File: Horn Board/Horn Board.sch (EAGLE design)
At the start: 11 parts, among them K1 RELAY-SPDT-JZC-11F, T1 2N2222

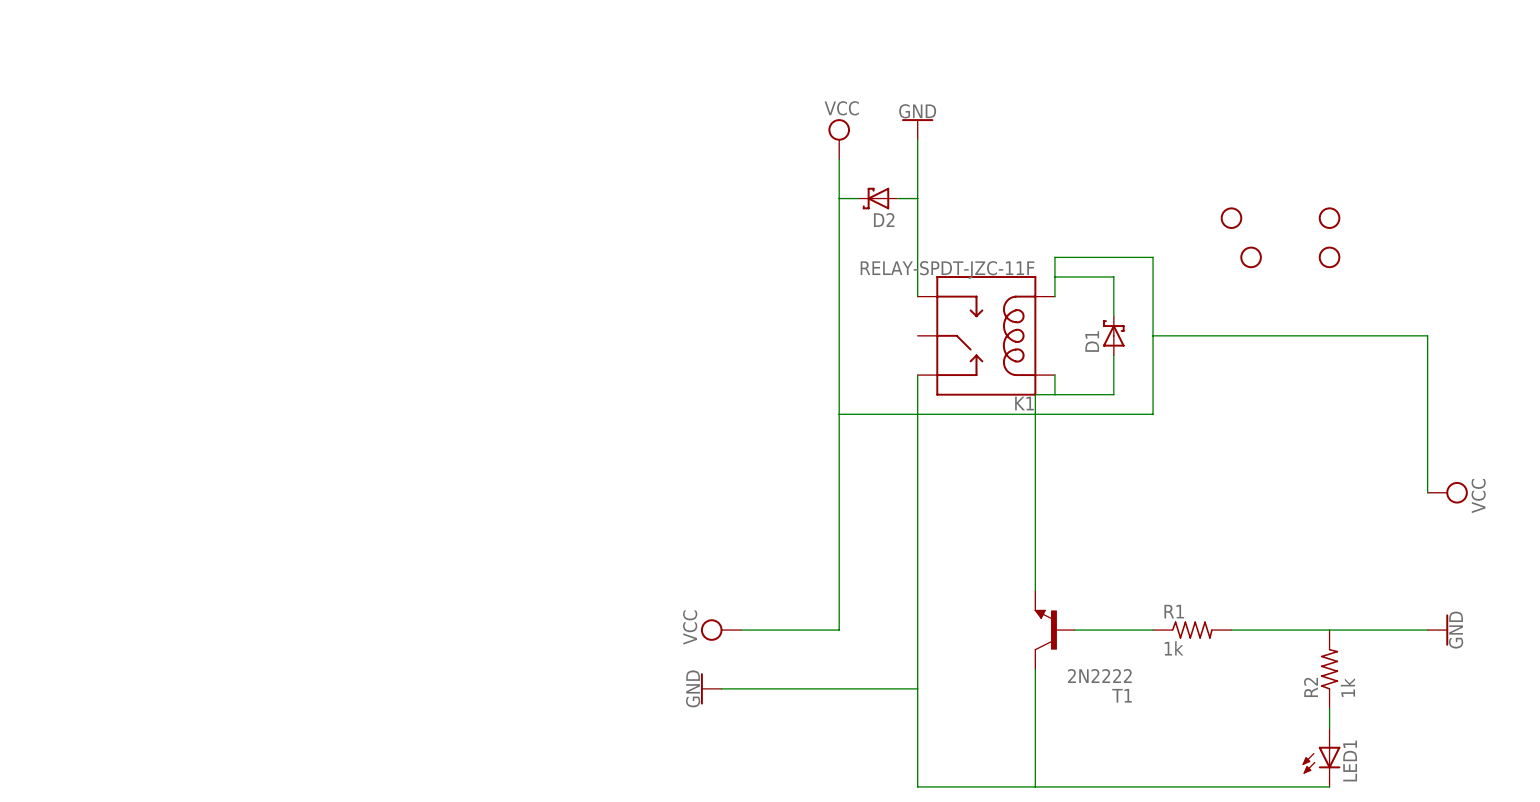
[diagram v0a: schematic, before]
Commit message: Added Connectors to horn board
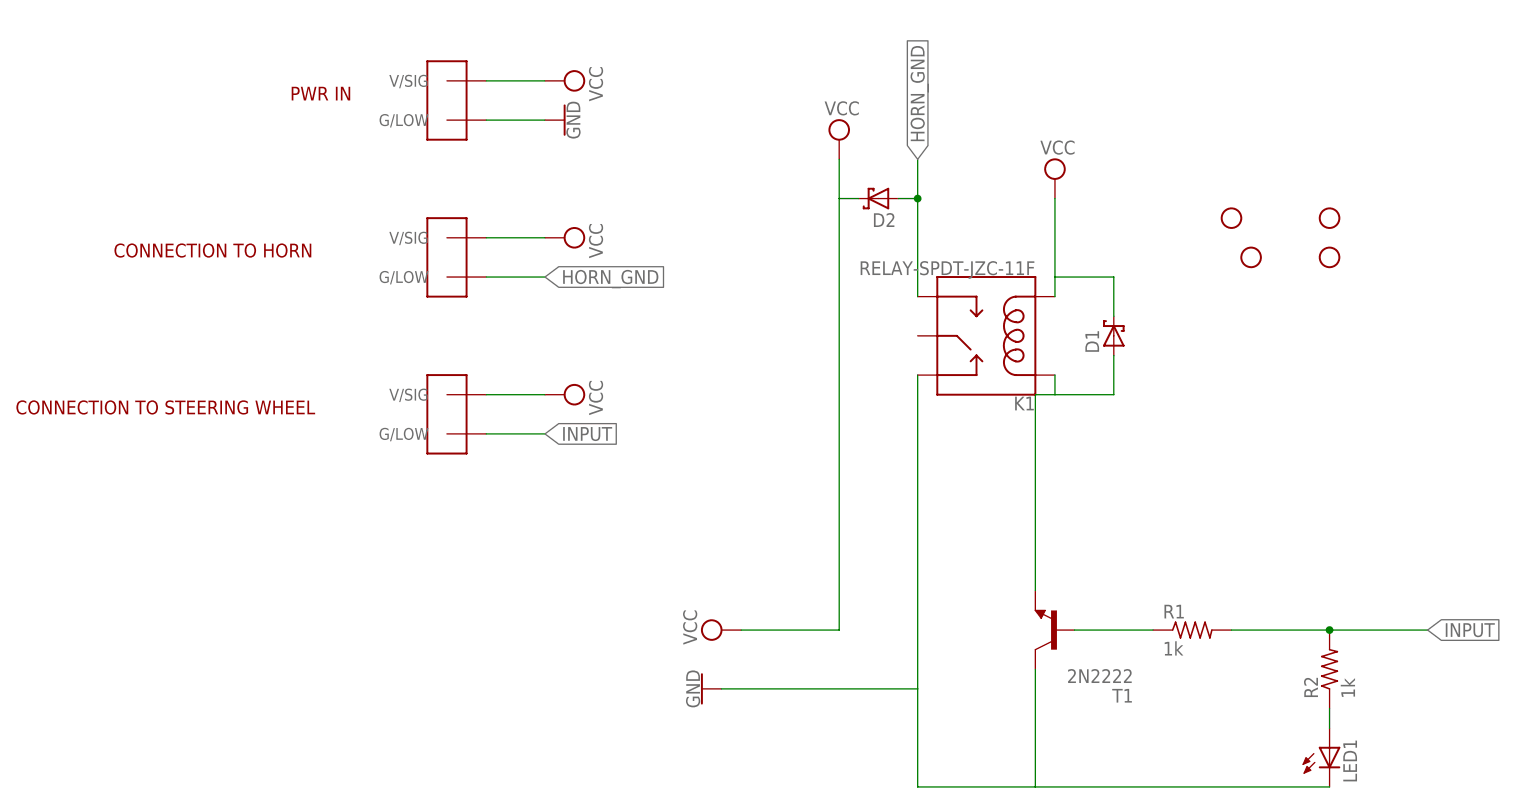
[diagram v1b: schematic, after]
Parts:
- added U$1, U$2, U$8: TE770966, Shell2013(1):TE770966
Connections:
- new net HORN_GND: D2.A, K1.NO, U$1.G/LOW
- new net INPUT: R1.2, R2.2, U$2.G/LOW
- net GND: now also U$8.G/LOW; no longer D2.A, K1.NO, R1.2, R2.2
- net VCC: now also U$1.V/SIG, U$2.V/SIG, U$8.V/SIG
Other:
- note added: "CONNECTION TO HORN"
- note added: "CONNECTION TO STEERING WHEEL"
- note added: "PWR IN"
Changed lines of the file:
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@@
 <?xml version="1.0" encoding="utf-8"?>
 <!DOCTYPE eagle SYSTEM "eagle.dtd">
-<eagle version="8.3.2">
+<eagle version="8.4.1">
 <drawing>
 <settings>
@@
 <layers>
 <layer number="1" name="Top" color="4" fill="1" visible="no" active="no"/>
+<layer number="2" name="Route2" color="1" fill="3" visible="no" active="no"/>
+<layer number="3" name="Route3" color="4" fill="3" visible="no" active="no"/>
+<layer number="14" name="Route14" color="1" fill="6" visible="no" active="no"/>
+<layer number="15" name="Route15" color="4" fill="6" visible="no" active="no"/>
 <layer number="16" name="Bottom" color="1" fill="1" visible="no" active="no"/>
 <layer number="17" name="Pads" color="2" fill="1" visible="no" active="no"/>
@@
 <part name="R2" library="adafruit" library_urn="urn:adsk.eagle:library:420" deviceset="R-US_" device="0204/2V" value="1k"/>
 <part name="T1" library="adafruit" library_urn="urn:adsk.eagle:library:420" deviceset="2N2222" device=""/>
-<part name="SUPPLY4" library="supply2" library_urn="urn:adsk.eagle:library:372" deviceset="VCC" device=""/>
 <part name="SUPPLY5" library="supply2" library_urn="urn:adsk.eagle:library:372" deviceset="VCC" device=""/>
 <part name="SUPPLY6" library="supply2" library_urn="urn:adsk.eagle:library:372" deviceset="VCC" device=""/>
-<part name="GND1" library="SparkFun-PowerSymbols" library_urn="urn:adsk.eagle:library:530" deviceset="GND" device=""/>
 <part name="GND2" library="SparkFun-PowerSymbols" library_urn="urn:adsk.eagle:library:530" deviceset="GND" device=""/>
-<part name="GND3" library="SparkFun-PowerSymbols" library_urn="urn:adsk.eagle:library:530" deviceset="GND" device=""/>
 <part name="H1" library="SparkFun-Hardware" library_urn="urn:adsk.eagle:library:519" deviceset="STAND-OFF" device="" package3d_urn="urn:adsk.eagle:package:38630/1"/>
 <part name="H2" library="SparkFun-Hardware" library_urn="urn:adsk.eagle:library:519" deviceset="STAND-OFF" device="" package3d_urn="urn:adsk.eagle:package:38630/1"/>
 <part name="H3" library="SparkFun-Hardware" library_urn="urn:adsk.eagle:library:519" deviceset="STAND-OFF" device="" package3d_urn="urn:adsk.eagle:package:38630/1"/>
 <part name="H4" library="SparkFun-Hardware" library_urn="urn:adsk.eagle:library:519" deviceset="STAND-OFF" device="" package3d_urn="urn:adsk.eagle:package:38630/1"/>
+<part name="U$8" library="Shell2013(1)" deviceset="TE770966" device=""/>
+<part name="U$1" library="Shell2013(1)" deviceset="TE770966" device=""/>
+<part name="U$2" library="Shell2013(1)" deviceset="TE770966" device=""/>
+<part name="SUPPLY1" library="supply2" library_urn="urn:adsk.eagle:library:372" deviceset="VCC" device=""/>
+<part name="SUPPLY2" library="supply2" library_urn="urn:adsk.eagle:library:372" deviceset="VCC" device=""/>
+<part name="GND1" library="SparkFun-PowerSymbols" library_urn="urn:adsk.eagle:library:530" deviceset="GND" device=""/>
+<part name="SUPPLY3" library="supply2" library_urn="urn:adsk.eagle:library:372" deviceset="VCC" device=""/>
+<part name="SUPPLY4" library="supply2" library_urn="urn:adsk.eagle:library:372" deviceset="VCC" device=""/>
 </parts>
 <sheets>
 <sheet>
 <plain>
+<text x="-33.02" y="93.98" size="1.778" layer="94">PWR IN</text>
+<text x="-55.88" y="73.66" size="1.778" layer="94">CONNECTION TO HORN</text>
+<text x="-68.58" y="53.34" size="1.778" layer="94">CONNECTION TO STEERING WHEEL</text>
 </plain>
 <instances>
@@
 <instance part="R2" gate="G$1" x="101.6" y="20.32" rot="R90"/>
 <instance part="T1" gate="G$1" x="66.04" y="25.4" rot="R180"/>
-<instance part="SUPPLY4" gate="G$1" x="116.84" y="43.18" rot="R270"/>
 <instance part="SUPPLY5" gate="G$1" x="22.86" y="25.4" rot="R90"/>
 <instance part="SUPPLY6" gate="G$1" x="38.1" y="88.9"/>
-<instance part="GND1" gate="1" x="48.26" y="91.44" rot="R180"/>
 <instance part="GND2" gate="1" x="20.32" y="17.78" rot="R270"/>
-<instance part="GND3" gate="1" x="116.84" y="25.4" rot="R90"/>
 <instance part="H1" gate="G$1" x="88.9" y="78.74"/>
 <instance part="H2" gate="G$1" x="101.6" y="78.74"/>
 <instance part="H3" gate="G$1" x="91.44" y="73.66"/>
 <instance part="H4" gate="G$1" x="101.6" y="73.66"/>
+<instance part="U$8" gate="G$1" x="-15.24" y="93.98" rot="R270"/>
+<instance part="U$1" gate="G$1" x="-15.24" y="73.66" rot="R270"/>
+<instance part="U$2" gate="G$1" x="-15.24" y="53.34" rot="R270"/>
+<instance part="SUPPLY1" gate="G$1" x="66.04" y="83.82"/>
+<instance part="SUPPLY2" gate="G$1" x="2.54" y="96.52" rot="R270"/>
+<instance part="GND1" gate="1" x="2.54" y="91.44" rot="R90"/>
+<instance part="SUPPLY3" gate="G$1" x="2.54" y="76.2" rot="R270"/>
+<instance part="SUPPLY4" gate="G$1" x="2.54" y="55.88" rot="R270"/>
 </instances>
 <busses>
@@
 <net name="VCC" class="0">
 <segment>
+<pinref part="SUPPLY6" gate="G$1" pin="VCC"/>
 <pinref part="D2" gate="G$1" pin="C"/>
-<pinref part="SUPPLY6" gate="G$1" pin="VCC"/>
 <wire x1="40.64" y1="81.28" x2="38.1" y2="81.28" width="0.1524" layer="91"/>
 <wire x1="38.1" y1="81.28" x2="38.1" y2="86.36" width="0.1524" layer="91"/>
+<wire x1="38.1" y1="25.4" x2="38.1" y2="81.28" width="0.1524" layer="91"/>
 <pinref part="SUPPLY5" gate="G$1" pin="VCC"/>
 <wire x1="25.4" y1="25.4" x2="38.1" y2="25.4" width="0.1524" layer="91"/>
-<wire x1="38.1" y1="25.4" x2="38.1" y2="53.34" width="0.1524" layer="91"/>
+</segment>
+<segment>
 <pinref part="K1" gate="K$1" pin="COIL2"/>
-<wire x1="38.1" y1="53.34" x2="38.1" y2="81.28" width="0.1524" layer="91"/>
 <wire x1="66.04" y1="68.58" x2="66.04" y2="71.12" width="0.1524" layer="91"/>
 <wire x1="66.04" y1="71.12" x2="73.66" y2="71.12" width="0.1524" layer="91"/>
 <pinref part="D1" gate="G$1" pin="C"/>
 <wire x1="73.66" y1="71.12" x2="73.66" y2="66.04" width="0.1524" layer="91"/>
-<wire x1="66.04" y1="71.12" x2="66.04" y2="73.66" width="0.1524" layer="91"/>
-<wire x1="66.04" y1="73.66" x2="78.74" y2="73.66" width="0.1524" layer="91"/>
-<wire x1="78.74" y1="73.66" x2="78.74" y2="63.5" width="0.1524" layer="91"/>
-<wire x1="78.74" y1="63.5" x2="78.74" y2="53.34" width="0.1524" layer="91"/>
-<wire x1="78.74" y1="53.34" x2="38.1" y2="53.34" width="0.1524" layer="91"/>
+<pinref part="SUPPLY1" gate="G$1" pin="VCC"/>
+<wire x1="66.04" y1="81.28" x2="66.04" y2="71.12" width="0.1524" layer="91"/>
+</segment>
+<segment>
+<pinref part="U$8" gate="G$1" pin="V/SIG"/>
+<wire x1="-7.62" y1="96.52" x2="0" y2="96.52" width="0.1524" layer="91"/>
+<pinref part="SUPPLY2" gate="G$1" pin="VCC"/>
+</segment>
+<segment>
+<pinref part="U$1" gate="G$1" pin="V/SIG"/>
+<wire x1="-7.62" y1="76.2" x2="0" y2="76.2" width="0.1524" layer="91"/>
+<pinref part="SUPPLY3" gate="G$1" pin="VCC"/>
+</segment>
+<segment>
+<pinref part="U$2" gate="G$1" pin="V/SIG"/>
+<wire x1="-7.62" y1="55.88" x2="0" y2="55.88" width="0.1524" layer="91"/>
 <pinref part="SUPPLY4" gate="G$1" pin="VCC"/>
-<wire x1="78.74" y1="63.5" x2="114.3" y2="63.5" width="0.1524" layer="91"/>
-<wire x1="114.3" y1="63.5" x2="114.3" y2="43.18" width="0.1524" layer="91"/>
 </segment>
 </net>
 <net name="GND" class="0">
-<segment>
-<pinref part="D2" gate="G$1" pin="A"/>
-<pinref part="K1" gate="K$1" pin="NO"/>
-<wire x1="45.72" y1="81.28" x2="48.26" y2="81.28" width="0.1524" layer="91"/>
-<wire x1="48.26" y1="81.28" x2="48.26" y2="68.58" width="0.1524" layer="91"/>
-<pinref part="GND1" gate="1" pin="GND"/>
-<wire x1="48.26" y1="81.28" x2="48.26" y2="88.9" width="0.1524" layer="91"/>
-</segment>
 <segment>
 <pinref part="GND2" gate="1" pin="GND"/>
@@
 </segment>
 <segment>
-<pinref part="R1" gate="G$1" pin="2"/>
-<pinref part="R2" gate="G$1" pin="2"/>
-<wire x1="88.9" y1="25.4" x2="101.6" y2="25.4" width="0.1524" layer="91"/>
-<pinref part="GND3" gate="1" pin="GND"/>
-<wire x1="101.6" y1="25.4" x2="114.3" y2="25.4" width="0.1524" layer="91"/>
+<pinref part="U$8" gate="G$1" pin="G/LOW"/>
+<wire x1="-7.62" y1="91.44" x2="0" y2="91.44" width="0.1524" layer="91"/>
+<pinref part="GND1" gate="1" pin="GND"/>
 </segment>
 </net>
@@
 </segment>
 </net>
+<net name="INPUT" class="0">
+<segment>
+<pinref part="R1" gate="G$1" pin="2"/>
+<pinref part="R2" gate="G$1" pin="2"/>
+<wire x1="88.9" y1="25.4" x2="101.6" y2="25.4" width="0.1524" layer="91"/>
+<wire x1="101.6" y1="25.4" x2="114.3" y2="25.4" width="0.1524" layer="91"/>
+<junction x="101.6" y="25.4"/>
+<label x="114.3" y="25.4" size="1.778" layer="95" xref="yes"/>
+</segment>
+<segment>
+<pinref part="U$2" gate="G$1" pin="G/LOW"/>
+<wire x1="-7.62" y1="50.8" x2="0" y2="50.8" width="0.1524" layer="91"/>
+<label x="0" y="50.8" size="1.778" layer="95" xref="yes"/>
+</segment>
+</net>
+<net name="HORN_GND" class="0">
+<segment>
+<pinref part="K1" gate="K$1" pin="NO"/>
+<wire x1="48.26" y1="68.58" x2="48.26" y2="81.28" width="0.1524" layer="91"/>
+<pinref part="D2" gate="G$1" pin="A"/>
+<wire x1="48.26" y1="81.28" x2="48.26" y2="86.36" width="0.1524" layer="91"/>
+<wire x1="45.72" y1="81.28" x2="48.26" y2="81.28" width="0.1524" layer="91"/>
+<junction x="48.26" y="81.28"/>
+<label x="48.26" y="86.36" size="1.778" layer="95" rot="R90" xref="yes"/>
+</segment>
+<segment>
+<pinref part="U$1" gate="G$1" pin="G/LOW"/>
+<wire x1="-7.62" y1="71.12" x2="0" y2="71.12" width="0.1524" layer="91"/>
+<label x="0" y="71.12" size="1.778" layer="95" xref="yes"/>
+</segment>
+</net>
